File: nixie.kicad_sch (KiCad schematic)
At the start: 2 parts

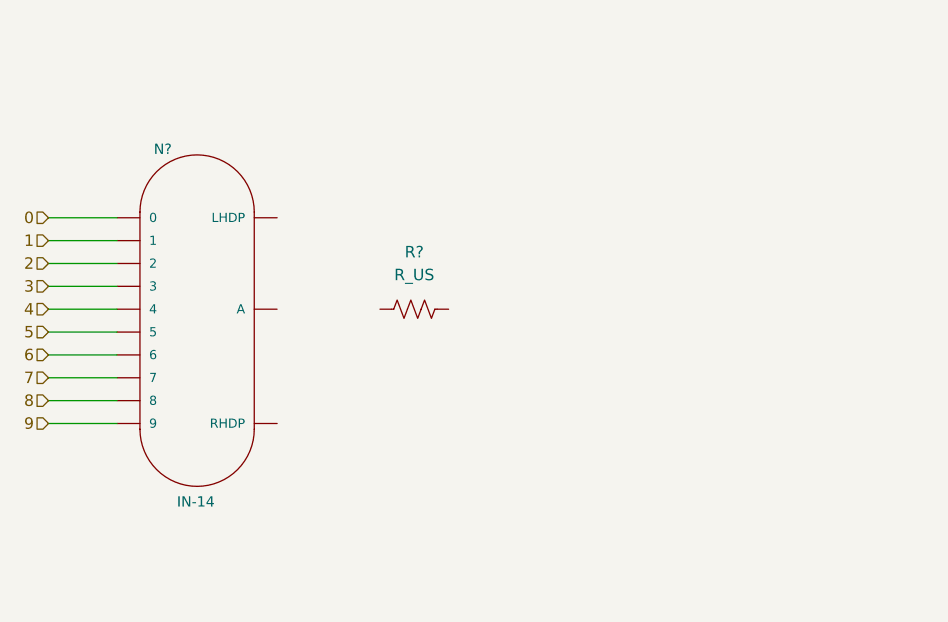
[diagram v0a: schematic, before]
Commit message: updated the nixie schematic
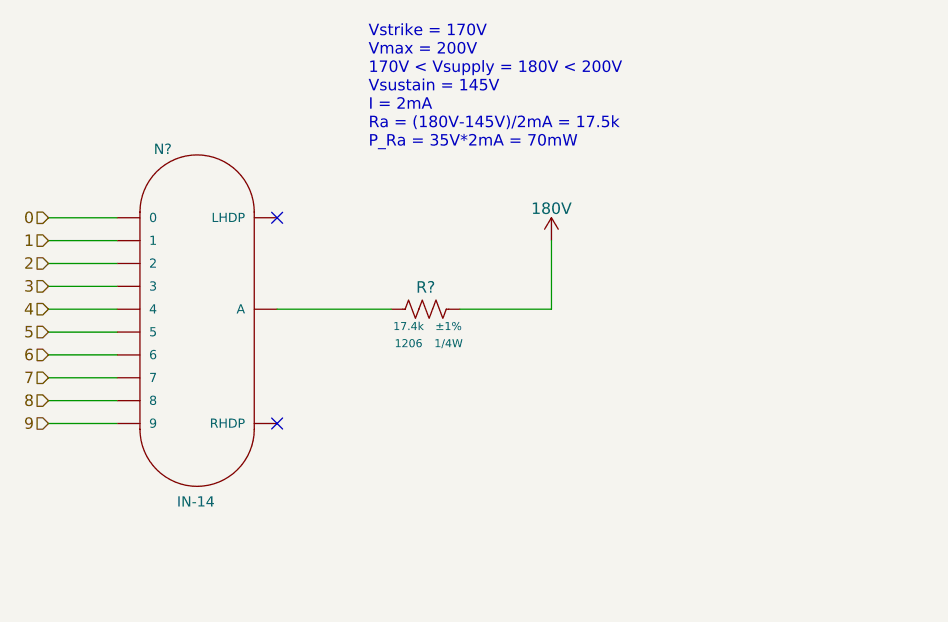
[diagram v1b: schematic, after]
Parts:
- removed R?: R_US, Resistor_SMD:R_1206_3216Metric_Pad1.30x1.75mm_HandSolder, symbol Device:R_US
- added R?: R_17K4_1P_1/4W_1206, Resistor_SMD:R_1206_3216Metric, symbol arjun_symbols:R_17K4_1P_1/4W_1206
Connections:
- net at N?.A: now also R?.2
- new net 180V: R?.1
- no-connect marks 0 -> 2
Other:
- note added: "Vstrike = 170V Vmax = 200V 170V < Vsupply = 180V < 200V Vsustain = 145V I = 2mA Ra = (180V-145V)/2mA = 17.5k P_Ra = 35V*2mA = 70mW"
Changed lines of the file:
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@@
 (kicad_sch (version 20211123) (generator eeschema)
   (paper "A4")
+  (no_connect (at 124.46 81.28))
+  (no_connect (at 124.46 104.14))
   (wire (pts (xy 99.06 83.82) (xy 106.68 83.82))
+    (stroke (width 0) (type default) (color 0 0 0 0))
+  )
+  (wire (pts (xy 124.46 91.44) (xy 137.16 91.44))
     (stroke (width 0) (type default) (color 0 0 0 0))
   )
@@
     (stroke (width 0) (type default) (color 0 0 0 0))
   )
+  (wire (pts (xy 154.94 91.44) (xy 154.94 83.82))
+    (stroke (width 0) (type default) (color 0 0 0 0))
+  )
   (wire (pts (xy 99.06 86.36) (xy 106.68 86.36))
     (stroke (width 0) (type default) (color 0 0 0 0))
   )
   (wire (pts (xy 99.06 93.98) (xy 106.68 93.98))
+    (stroke (width 0) (type default) (color 0 0 0 0))
+  )
+  (wire (pts (xy 144.78 91.44) (xy 154.94 91.44))
     (stroke (width 0) (type default) (color 0 0 0 0))
   )
@@
   (wire (pts (xy 99.06 88.9) (xy 106.68 88.9))
     (stroke (width 0) (type default) (color 0 0 0 0))
+  )
+  (text "Vstrike = 170V\nVmax = 200V\n170V < Vsupply = 180V < 200V\nVsustain = 145V\nI = 2mA\nRa = (180V-145V)/2mA = 17.5k\nP_Ra = 35V*2mA = 70mW"
+    (at 134.62 73.66 0)
+    (effects (font (size 1.27 1.27)) (justify left bottom))
   )
   (hierarchical_label "1" (shape input) (at 99.06 83.82 180)
@@
   (hierarchical_label "5" (shape input) (at 99.06 93.98 180)
     (effects (font (size 1.27 1.27)) (justify right))
+  )
+  (symbol (lib_id "arjun_symbols:180V") (at 154.94 83.82 0) (unit 1)
+    (in_bom yes) (on_board yes)
+    (property "Reference" "#PWR?" (id 0) (at 154.94 87.63 0)
+      (effects (font (size 1.27 1.27)) hide)
+    )
+    (property "Value" "180V" (id 1) (at 154.94 80.264 0))
+    (property "Footprint" "" (id 2) (at 154.94 83.82 0)
+      (effects (font (size 1.27 1.27)) hide)
+    )
+    (property "Datasheet" "" (id 3) (at 154.94 83.82 0)
+      (effects (font (size 1.27 1.27)) hide)
+    )
+    (pin "1")
   )
   (symbol (lib_id "arjun_symbols:IN-14") (at 106.68 81.28 0) (unit 1)
@@
     (pin "RHDP")
   )
-  (symbol (lib_id "Device:R_US") (at 139.7 91.44 270) (unit 1)
-    (in_bom yes) (on_board yes) (fields_autoplaced)
-    (property "Reference" "R?" (id 0) (at 139.7 85.09 90))
-    (property "Value" "R_US" (id 1) (at 139.7 87.63 90))
-    (property "Footprint" "Resistor_SMD:R_1206_3216Metric_Pad1.30x1.75mm_HandSolder" (id 2) (at 139.446 92.456 90)
+  (symbol (lib_id "arjun_symbols:R_17K4_1P_1{slash}4W_1206") (at 140.97 91.44 270) (unit 1)
+    (in_bom yes) (on_board yes)
+    (property "Reference" "R?" (id 0) (at 140.97 88.265 90)
+      (effects (font (size 1.27 1.27)) (justify top))
+    )
+    (property "Value" "R_17K4_1P_1/4W_1206" (id 1) (at 140.97 83.82 90)
       (effects (font (size 1.27 1.27)) hide)
     )
-    (property "Datasheet" "~" (id 3) (at 139.7 91.44 0)
+    (property "Footprint" "Resistor_SMD:R_1206_3216Metric" (id 2) (at 138.43 81.28 90)
       (effects (font (size 1.27 1.27)) hide)
     )
+    (property "Datasheet" "https://www.yageo.com/upload/media/product/productsearch/datasheet/rchip/PYu-RC_Group_51_RoHS_L_12.pdf" (id 3) (at 115.57 86.36 0)
+      (effects (font (size 1.27 1.27)) hide)
+    )
+    (property "Resistance" "17.4k" (id 4) (at 139.065 93.345 90)
+      (effects (font (size 0.889 0.889)))
+    )
+    (property "Tolerance" "±1% " (id 5) (at 143.51 93.345 90)
+      (effects (font (size 0.889 0.889)))
+    )
+    (property "Package" "1206" (id 6) (at 139.065 95.25 90)
+      (effects (font (size 0.889 0.889)))
+    )
+    (property "Power" "1/4W" (id 7) (at 143.51 95.25 90)
+      (effects (font (size 0.889 0.889)))
+    )
     (pin "1")

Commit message: wired up Nixie tubes
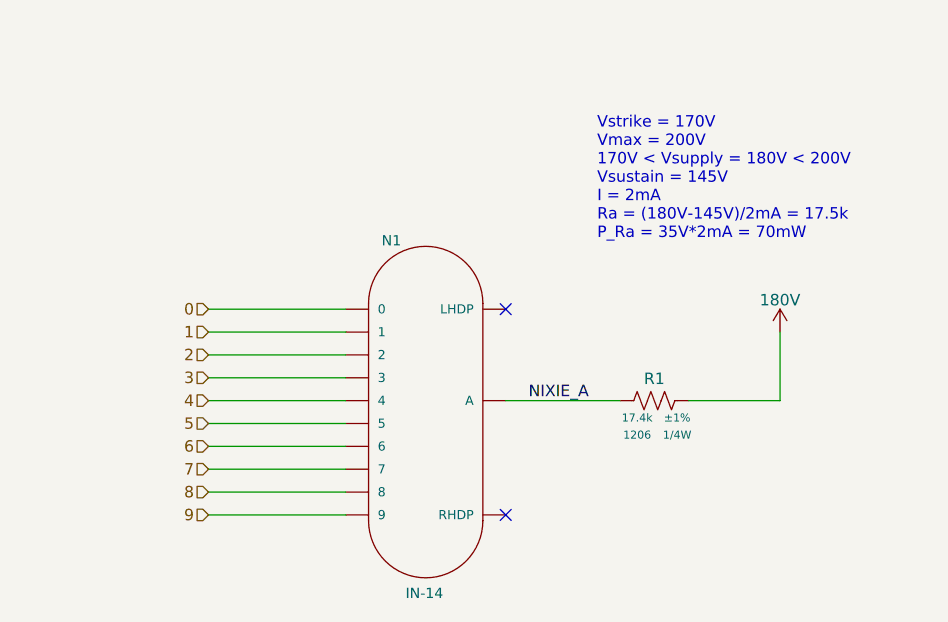
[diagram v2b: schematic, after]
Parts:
- gave numbers to parts that had none: 2
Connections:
- net NIXIE_A: now reaches N1.A, R1.2
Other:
- moved on the sheet: N1, R1
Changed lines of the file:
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@@
 (kicad_sch (version 20211123) (generator eeschema)
   (paper "A4")
-  (no_connect (at 124.46 81.28))
-  (no_connect (at 124.46 104.14))
-  (wire (pts (xy 99.06 83.82) (xy 106.68 83.82))
+  (no_connect (at 149.86 91.44))
+  (no_connect (at 149.86 114.3))
+  (wire (pts (xy 116.84 93.98) (xy 132.08 93.98))
     (stroke (width 0) (type default) (color 0 0 0 0))
   )
-  (wire (pts (xy 124.46 91.44) (xy 137.16 91.44))
+  (wire (pts (xy 149.86 101.6) (xy 162.56 101.6))
     (stroke (width 0) (type default) (color 0 0 0 0))
   )
-  (wire (pts (xy 99.06 101.6) (xy 106.68 101.6))
+  (wire (pts (xy 116.84 111.76) (xy 132.08 111.76))
     (stroke (width 0) (type default) (color 0 0 0 0))
   )
-  (wire (pts (xy 99.06 99.06) (xy 106.68 99.06))
+  (wire (pts (xy 116.84 109.22) (xy 132.08 109.22))
     (stroke (width 0) (type default) (color 0 0 0 0))
   )
-  (wire (pts (xy 99.06 81.28) (xy 106.68 81.28))
+  (wire (pts (xy 116.84 91.44) (xy 132.08 91.44))
     (stroke (width 0) (type default) (color 0 0 0 0))
   )
-  (wire (pts (xy 99.06 96.52) (xy 106.68 96.52))
+  (wire (pts (xy 116.84 106.68) (xy 132.08 106.68))
     (stroke (width 0) (type default) (color 0 0 0 0))
   )
-  (wire (pts (xy 154.94 91.44) (xy 154.94 83.82))
+  (wire (pts (xy 180.34 101.6) (xy 180.34 93.98))
     (stroke (width 0) (type default) (color 0 0 0 0))
   )
-  (wire (pts (xy 99.06 86.36) (xy 106.68 86.36))
+  (wire (pts (xy 116.84 96.52) (xy 132.08 96.52))
     (stroke (width 0) (type default) (color 0 0 0 0))
   )
-  (wire (pts (xy 99.06 93.98) (xy 106.68 93.98))
+  (wire (pts (xy 116.84 104.14) (xy 132.08 104.14))
     (stroke (width 0) (type default) (color 0 0 0 0))
   )
-  (wire (pts (xy 144.78 91.44) (xy 154.94 91.44))
+  (wire (pts (xy 170.18 101.6) (xy 180.34 101.6))
     (stroke (width 0) (type default) (color 0 0 0 0))
   )
-  (wire (pts (xy 99.06 91.44) (xy 106.68 91.44))
+  (wire (pts (xy 116.84 101.6) (xy 132.08 101.6))
     (stroke (width 0) (type default) (color 0 0 0 0))
   )
-  (wire (pts (xy 99.06 104.14) (xy 106.68 104.14))
+  (wire (pts (xy 116.84 114.3) (xy 132.08 114.3))
     (stroke (width 0) (type default) (color 0 0 0 0))
   )
-  (wire (pts (xy 99.06 88.9) (xy 106.68 88.9))
+  (wire (pts (xy 116.84 99.06) (xy 132.08 99.06))
     (stroke (width 0) (type default) (color 0 0 0 0))
   )
   (text "Vstrike = 170V\nVmax = 200V\n170V < Vsupply = 180V < 200V\nVsustain = 145V\nI = 2mA\nRa = (180V-145V)/2mA = 17.5k\nP_Ra = 35V*2mA = 70mW"
-    (at 134.62 73.66 0)
+    (at 160.02 83.82 0)
     (effects (font (size 1.27 1.27)) (justify left bottom))
   )
-  (hierarchical_label "1" (shape input) (at 99.06 83.82 180)
+  (label "NIXIE_A" (at 152.4 101.6 0)
+    (effects (font (size 1.27 1.27)) (justify left bottom))
+  )
+  (hierarchical_label "1" (shape input) (at 116.84 93.98 180)
     (effects (font (size 1.27 1.27)) (justify right))
   )
-  (hierarchical_label "9" (shape input) (at 99.06 104.14 180)
+  (hierarchical_label "9" (shape input) (at 116.84 114.3 180)
     (effects (font (size 1.27 1.27)) (justify right))
   )
-  (hierarchical_label "6" (shape input) (at 99.06 96.52 180)
+  (hierarchical_label "6" (shape input) (at 116.84 106.68 180)
     (effects (font (size 1.27 1.27)) (justify right))
   )
-  (hierarchical_label "8" (shape input) (at 99.06 101.6 180)
+  (hierarchical_label "8" (shape input) (at 116.84 111.76 180)
     (effects (font (size 1.27 1.27)) (justify right))
   )
-  (hierarchical_label "3" (shape input) (at 99.06 88.9 180)
+  (hierarchical_label "3" (shape input) (at 116.84 99.06 180)
     (effects (font (size 1.27 1.27)) (justify right))
   )
-  (hierarchical_label "2" (shape input) (at 99.06 86.36 180)
+  (hierarchical_label "2" (shape input) (at 116.84 96.52 180)
     (effects (font (size 1.27 1.27)) (justify right))
   )
-  (hierarchical_label "7" (shape input) (at 99.06 99.06 180)
+  (hierarchical_label "7" (shape input) (at 116.84 109.22 180)
     (effects (font (size 1.27 1.27)) (justify right))
   )
-  (hierarchical_label "0" (shape input) (at 99.06 81.28 180)
+  (hierarchical_label "0" (shape input) (at 116.84 91.44 180)
     (effects (font (size 1.27 1.27)) (justify right))
   )
-  (hierarchical_label "4" (shape input) (at 99.06 91.44 180)
+  (hierarchical_label "4" (shape input) (at 116.84 101.6 180)
     (effects (font (size 1.27 1.27)) (justify right))
   )
-  (hierarchical_label "5" (shape input) (at 99.06 93.98 180)
+  (hierarchical_label "5" (shape input) (at 116.84 104.14 180)
     (effects (font (size 1.27 1.27)) (justify right))
   )
-  (symbol (lib_id "arjun_symbols:180V") (at 154.94 83.82 0) (unit 1)
+  (symbol (lib_id "arjun_symbols:180V") (at 180.34 93.98 0) (unit 1)
     (in_bom yes) (on_board yes)
-    (property "Reference" "#PWR?" (id 0) (at 154.94 87.63 0)
+    (property "Reference" "#PWR0101" (id 0) (at 180.34 97.79 0)
       (effects (font (size 1.27 1.27)) hide)
     )
-    (property "Value" "180V" (id 1) (at 154.94 80.264 0))
-    (property "Footprint" "" (id 2) (at 154.94 83.82 0)
+    (property "Value" "180V" (id 1) (at 180.34 90.424 0))
+    (property "Footprint" "" (id 2) (at 180.34 93.98 0)
       (effects (font (size 1.27 1.27)) hide)
     )
-    (property "Datasheet" "" (id 3) (at 154.94 83.82 0)
+    (property "Datasheet" "" (id 3) (at 180.34 93.98 0)
       (effects (font (size 1.27 1.27)) hide)
     )
     (pin "1")
   )
-  (symbol (lib_id "arjun_symbols:IN-14") (at 106.68 81.28 0) (unit 1)
+  (symbol (lib_id "arjun_symbols:IN-14") (at 132.08 91.44 0) (unit 1)
     (in_bom yes) (on_board yes)
-    (property "Reference" "N?" (id 0) (at 111.76 73.66 0)
+    (property "Reference" "N1" (id 0) (at 137.16 83.82 0)
       (effects (font (size 1.143 1.143)))
     )
-    (property "Value" "IN-14" (id 1) (at 115.4258 112.841 0)
+    (property "Value" "IN-14" (id 1) (at 140.8258 123.001 0)
       (effects (font (size 1.143 1.143)))
     )
-    (property "Footprint" "arjun_footprints:IN-14" (id 2) (at 107.442 77.47 0)
+    (property "Footprint" "arjun_footprints:IN-14" (id 2) (at 132.842 87.63 0)
       (effects (font (size 0.508 0.508)) hide)
     )
-    (property "Datasheet" "https://tubehobby.com/datasheets/in14.pdf" (id 3) (at 106.68 109.22 0)
+    (property "Datasheet" "https://tubehobby.com/datasheets/in14.pdf" (id 3) (at 132.08 119.38 0)
       (effects (font (size 1.27 1.27)) hide)
     )
-    (property "Datasheet2" "http://www.tube-tester.com/sites/nixie/data/in-14/in-14.htm" (id 4) (at 106.68 111.76 0)
+    (property "Datasheet2" "http://www.tube-tester.com/sites/nixie/data/in-14/in-14.htm" (id 4) (at 132.08 121.92 0)
       (effects (font (size 1.27 1.27)) hide)
     )
-    (property "Datasheet3" "http://www.tube-tester.com/sites/nixie/dat_arch/IN-14_01.pdf" (id 5) (at 106.68 106.68 0)
+    (property "Datasheet3" "http://www.tube-tester.com/sites/nixie/dat_arch/IN-14_01.pdf" (id 5) (at 132.08 116.84 0)
       (effects (font (size 1.27 1.27)) hide)
     )
@@
     (pin "RHDP")
   )
-  (symbol (lib_id "arjun_symbols:R_17K4_1P_1{slash}4W_1206") (at 140.97 91.44 270) (unit 1)
+  (symbol (lib_id "arjun_symbols:R_17K4_1P_1{slash}4W_1206") (at 166.37 101.6 270) (unit 1)
     (in_bom yes) (on_board yes)
-    (property "Reference" "R?" (id 0) (at 140.97 88.265 90)
+    (property "Reference" "R1" (id 0) (at 166.37 98.425 90)
       (effects (font (size 1.27 1.27)) (justify top))
     )
-    (property "Value" "R_17K4_1P_1/4W_1206" (id 1) (at 140.97 83.82 90)
+    (property "Value" "R_17K4_1P_1/4W_1206" (id 1) (at 166.37 93.98 90)
       (effects (font (size 1.27 1.27)) hide)
     )
-    (property "Footprint" "Resistor_SMD:R_1206_3216Metric" (id 2) (at 138.43 81.28 90)
+    (property "Footprint" "Resistor_SMD:R_1206_3216Metric" (id 2) (at 163.83 91.44 90)
       (effects (font (size 1.27 1.27)) hide)
     )
-    (property "Datasheet" "https://www.yageo.com/upload/media/product/productsearch/datasheet/rchip/PYu-RC_Group_51_RoHS_L_12.pdf" (id 3) (at 115.57 86.36 0)
+    (property "Datasheet" "https://www.yageo.com/upload/media/product/productsearch/datasheet/rchip/PYu-RC_Group_51_RoHS_L_12.pdf" (id 3) (at 140.97 96.52 0)
       (effects (font (size 1.27 1.27)) hide)
     )
-    (property "Resistance" "17.4k" (id 4) (at 139.065 93.345 90)
+    (property "Resistance" "17.4k" (id 4) (at 164.465 103.505 90)
       (effects (font (size 0.889 0.889)))
     )
-    (property "Tolerance" "±1% " (id 5) (at 143.51 93.345 90)
+    (property "Tolerance" "±1% " (id 5) (at 168.91 103.505 90)
       (effects (font (size 0.889 0.889)))
     )
-    (property "Package" "1206" (id 6) (at 139.065 95.25 90)
+    (property "Package" "1206" (id 6) (at 164.465 105.41 90)
       (effects (font (size 0.889 0.889)))
     )
-    (property "Power" "1/4W" (id 7) (at 143.51 95.25 90)
+    (property "Power" "1/4W" (id 7) (at 168.91 105.41 90)
       (effects (font (size 0.889 0.889)))
     )

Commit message: Added level shifter and finished up HV Shift Register page
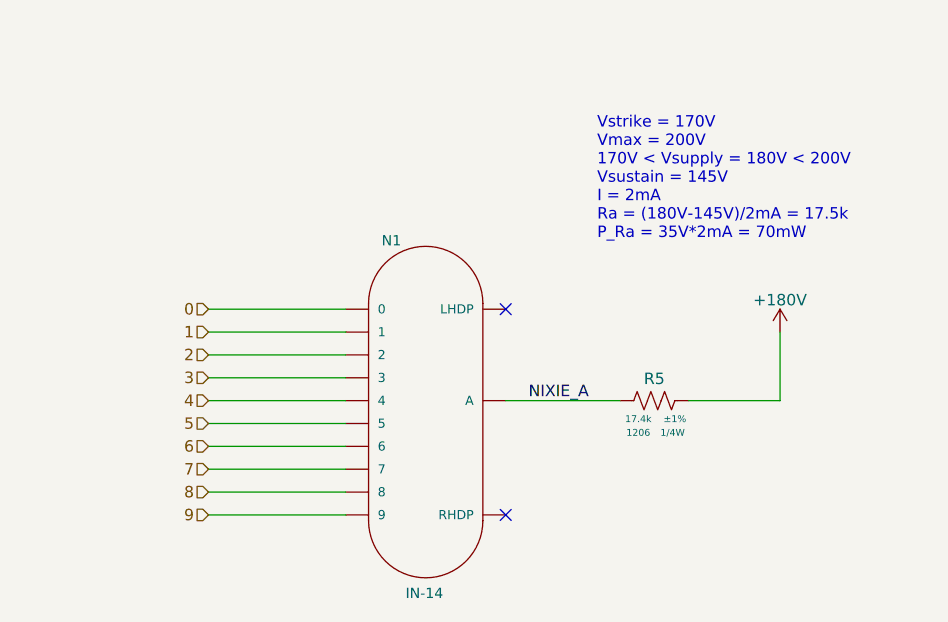
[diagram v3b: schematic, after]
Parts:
- removed R1: R_17K4_1P_1/4W_1206, Resistor_SMD:R_1206_3216Metric, symbol arjun_symbols:R_17K4_1P_1/4W_1206
- added R5: RES_17K4_1P_1/4W_1206, Resistor_SMD:R_1206_3216Metric, symbol arjun_symbols:RES_17K4_1P_1/4W_1206
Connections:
- net 180V: now also R5.1
- net NIXIE_A: now also R5.2
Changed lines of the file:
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@@
     (effects (font (size 1.27 1.27)) (justify right))
   )
-  (symbol (lib_id "arjun_symbols:180V") (at 180.34 93.98 0) (unit 1)
+  (symbol (lib_id "arjun_symbols:RES_17K4_1P_1{slash}4W_1206") (at 170.18 101.6 270) (unit 1)
     (in_bom yes) (on_board yes)
-    (property "Reference" "#PWR0101" (id 0) (at 180.34 97.79 0)
-      (effects (font (size 1.27 1.27)) hide)
+    (property "Reference" "R5" (id 0) (at 166.37 98.425 90)
+      (effects (font (size 1.27 1.27)) (justify top))
     )
-    (property "Value" "180V" (id 1) (at 180.34 90.424 0))
-    (property "Footprint" "" (id 2) (at 180.34 93.98 0)
-      (effects (font (size 1.27 1.27)) hide)
+    (property "Value" "RES_17K4_1P_1/4W_1206" (id 1) (at 175.26 109.22 0)
+      (effects (font (size 1.27 1.27)) (justify left) hide)
     )
-    (property "Datasheet" "" (id 3) (at 180.34 93.98 0)
-      (effects (font (size 1.27 1.27)) hide)
+    (property "Footprint" "Resistor_SMD:R_1206_3216Metric" (id 2) (at 172.72 109.22 0)
+      (effects (font (size 1.27 1.27)) (justify left) hide)
+    )
+    (property "Datasheet" "https://www.yageo.com/upload/media/product/productsearch/datasheet/rchip/PYu-RC_Group_51_RoHS_L_12.pdf" (id 3) (at 162.56 109.22 0)
+      (effects (font (size 1.27 1.27)) (justify left) hide)
+    )
+    (property "Manufacturer" "YAGEO" (id 4) (at 167.64 109.22 0)
+      (effects (font (size 1.27 1.27)) (justify left) hide)
+    )
+    (property "ManufacturerPN" "RC1206FR-0717K4L" (id 5) (at 165.1 109.22 0)
+      (effects (font (size 1.27 1.27)) (justify left) hide)
+    )
+    (property "Vendor" "Digi-Key" (id 6) (at 160.02 109.22 0)
+      (effects (font (size 1.27 1.27)) (justify left) hide)
+    )
+    (property "VendorPN" "311-17.4KFRCT-ND" (id 7) (at 157.48 109.22 0)
+      (effects (font (size 1.27 1.27)) (justify left) hide)
+    )
+    (property "Resistance" "17.4k" (id 8) (at 164.592 103.632 90)
+      (effects (font (size 0.762 0.762)))
+    )
+    (property "Tolerance" "±1% " (id 9) (at 168.656 103.632 90)
+      (effects (font (size 0.762 0.762)))
+    )
+    (property "Package" "1206" (id 10) (at 164.592 105.156 90)
+      (effects (font (size 0.762 0.762)))
+    )
+    (property "Power" "1/4W" (id 11) (at 168.402 105.156 90)
+      (effects (font (size 0.762 0.762)))
     )
     (pin "1")
+    (pin "2")
   )
   (symbol (lib_id "arjun_symbols:IN-14") (at 132.08 91.44 0) (unit 1)
@@
     (pin "RHDP")
   )
-  (symbol (lib_id "arjun_symbols:R_17K4_1P_1{slash}4W_1206") (at 166.37 101.6 270) (unit 1)
+  (symbol (lib_id "arjun_symbols:+180V") (at 180.34 93.98 0) (unit 1)
     (in_bom yes) (on_board yes)
-    (property "Reference" "R1" (id 0) (at 166.37 98.425 90)
-      (effects (font (size 1.27 1.27)) (justify top))
-    )
-    (property "Value" "R_17K4_1P_1/4W_1206" (id 1) (at 166.37 93.98 90)
+    (property "Reference" "#PWR06" (id 0) (at 180.34 97.79 0)
       (effects (font (size 1.27 1.27)) hide)
     )
-    (property "Footprint" "Resistor_SMD:R_1206_3216Metric" (id 2) (at 163.83 91.44 90)
+    (property "Value" "+180V" (id 1) (at 180.34 90.424 0))
+    (property "Footprint" "" (id 2) (at 180.34 93.98 0)
       (effects (font (size 1.27 1.27)) hide)
     )
-    (property "Datasheet" "https://www.yageo.com/upload/media/product/productsearch/datasheet/rchip/PYu-RC_Group_51_RoHS_L_12.pdf" (id 3) (at 140.97 96.52 0)
+    (property "Datasheet" "" (id 3) (at 180.34 93.98 0)
       (effects (font (size 1.27 1.27)) hide)
     )
-    (property "Resistance" "17.4k" (id 4) (at 164.465 103.505 90)
-      (effects (font (size 0.889 0.889)))
-    )
-    (property "Tolerance" "±1% " (id 5) (at 168.91 103.505 90)
-      (effects (font (size 0.889 0.889)))
-    )
-    (property "Package" "1206" (id 6) (at 164.465 105.41 90)
-      (effects (font (size 0.889 0.889)))
-    )
-    (property "Power" "1/4W" (id 7) (at 168.91 105.41 90)
-      (effects (font (size 0.889 0.889)))
-    )
     (pin "1")
-    (pin "2")
   )
 )

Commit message: Added USBC Connector to power page
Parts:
- renumbered R5 to R1
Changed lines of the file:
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@@
   (symbol (lib_id "arjun_symbols:RES_17K4_1P_1{slash}4W_1206") (at 170.18 101.6 270) (unit 1)
     (in_bom yes) (on_board yes)
-    (property "Reference" "R5" (id 0) (at 166.37 98.425 90)
+    (property "Reference" "R1" (id 0) (at 166.37 98.425 90)
       (effects (font (size 1.27 1.27)) (justify top))
     )
